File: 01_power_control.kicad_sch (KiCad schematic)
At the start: 12 parts, among them J7 54-00129 BARREL 5V, Q19 AO3401A, U1 XIAO ESP32-C6 / 113991254, U2 SN74HC595PWR, U3 SN74HC595PWR

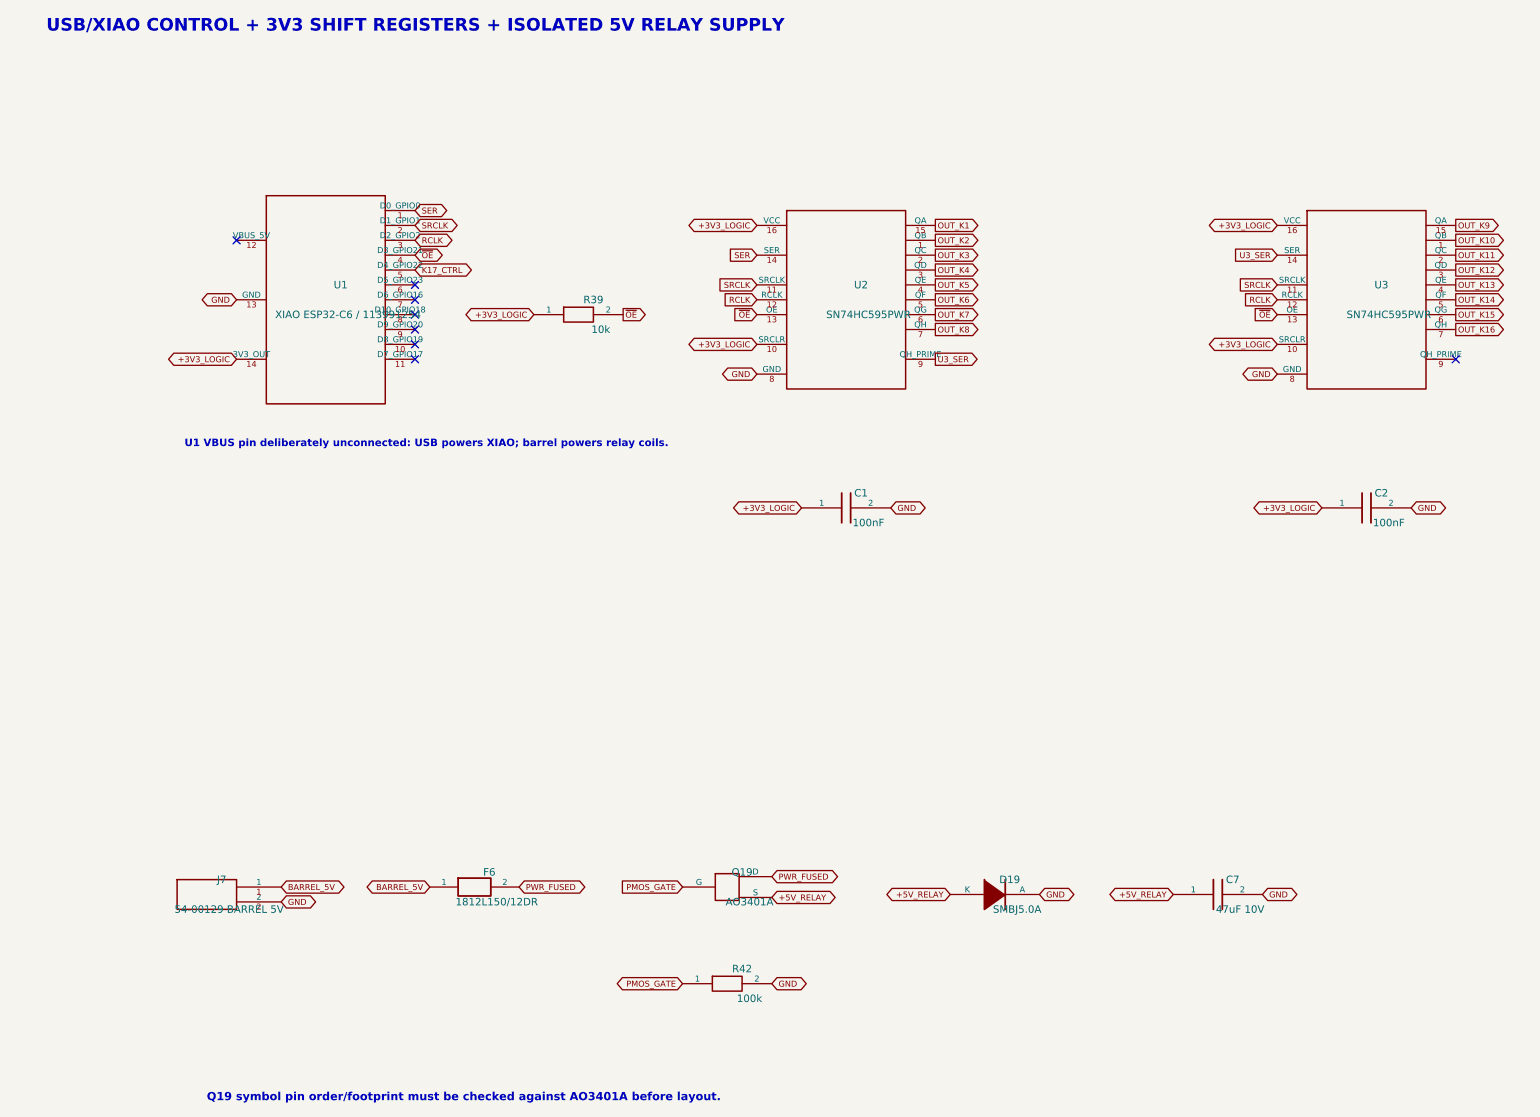
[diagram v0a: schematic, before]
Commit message: Add Phoenix 1190370 connector footprint
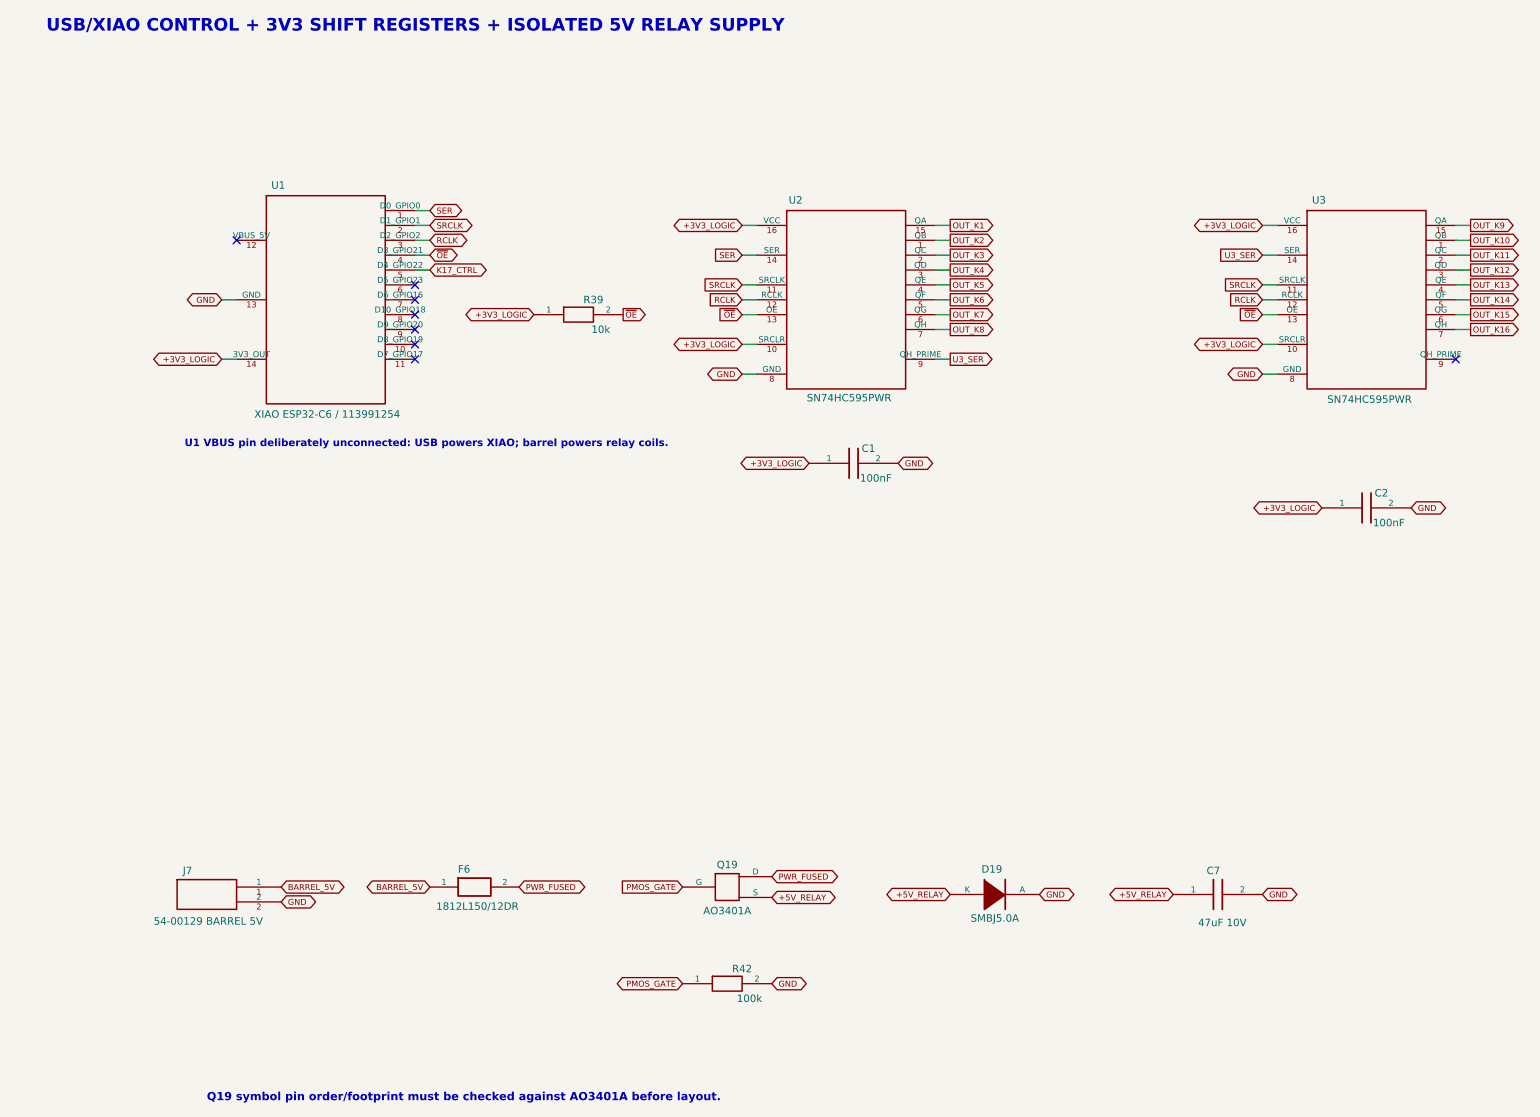
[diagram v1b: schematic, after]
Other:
- moved on the sheet: C1

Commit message: Import XIAO and Wurth vendor footprints
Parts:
- U1: footprint (none) -> Seeed_XIAO:XIAO-ESP32-C6-SMD
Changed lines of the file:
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@@
 			)
 		)
-		(property "Footprint" ""
+		(property "Footprint" "Seeed_XIAO:XIAO-ESP32-C6-SMD"
 			(at 63.5 63.5 0)
 			(hide yes)
@@
 			)
 		)
-		(property "Datasheet" ""
+		(property "Datasheet" "https://wiki.seeedstudio.com/xiao_esp32c6_getting_started/"
 			(at 63.5 63.5 0)
 			(hide yes)
@@
 			)
 		)
-		(property "Description" ""
+		(property "Description" "Seeed Studio XIAO ESP32-C6 module, castellated SMD mounting"
 			(at 63.5 63.5 0)
 			(show_name no)

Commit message: Assign custom footprints to schematic components
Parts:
- J7: footprint (none) -> BenchScan_Custom:Tensility_54-00129_DCJack
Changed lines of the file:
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@@
 			)
 		)
-		(property "Footprint" ""
+		(property "Footprint" "BenchScan_Custom:Tensility_54-00129_DCJack"
 			(at 43.18 165.1 0)
 			(hide yes)
@@
 			)
 		)
-		(property "Datasheet" ""
+		(property "Datasheet" "https://tensility.s3.us-west-2.amazonaws.com/imports/product_spec_sheets/54-00129.pdf"
 			(at 43.18 165.1 0)
 			(hide yes)
@@
 			)
 		)
-		(property "Description" ""
+		(property "Description" "Tensility 54-00129 right-angle 5.5/2.1 mm 6 A DC jack"
 			(at 43.18 165.1 0)
 			(show_name no)
